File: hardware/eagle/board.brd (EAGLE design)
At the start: 91.1 x 52.6 mm, 43 parts, among them IC1 TPS61165, IC2 TPS61165, Q1 12M, U1 24AA02, X1 MINI-USB-32005-301

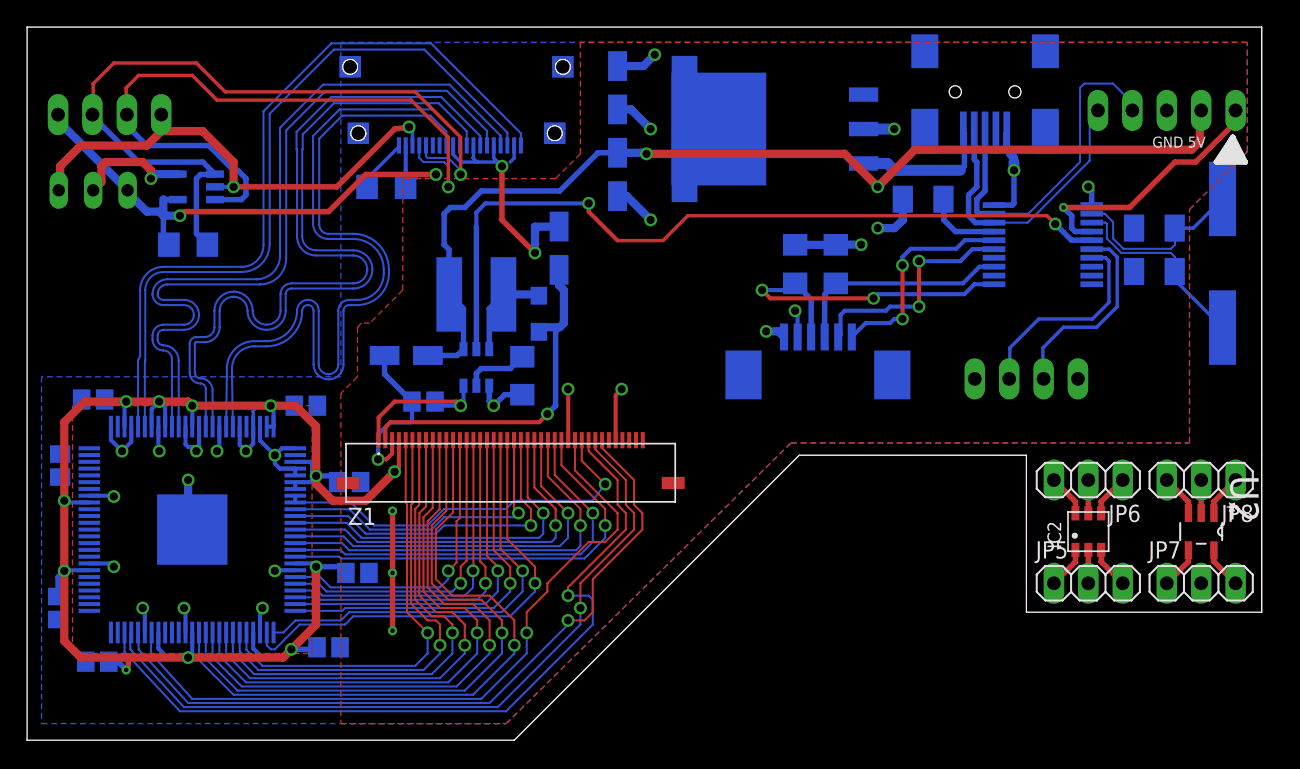
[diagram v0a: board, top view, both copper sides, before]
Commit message: Update Eagle files
Tweaked design to shrink the PCB, remove
backlight buttons, and removed the diode
on MCLR for the microcontroller.
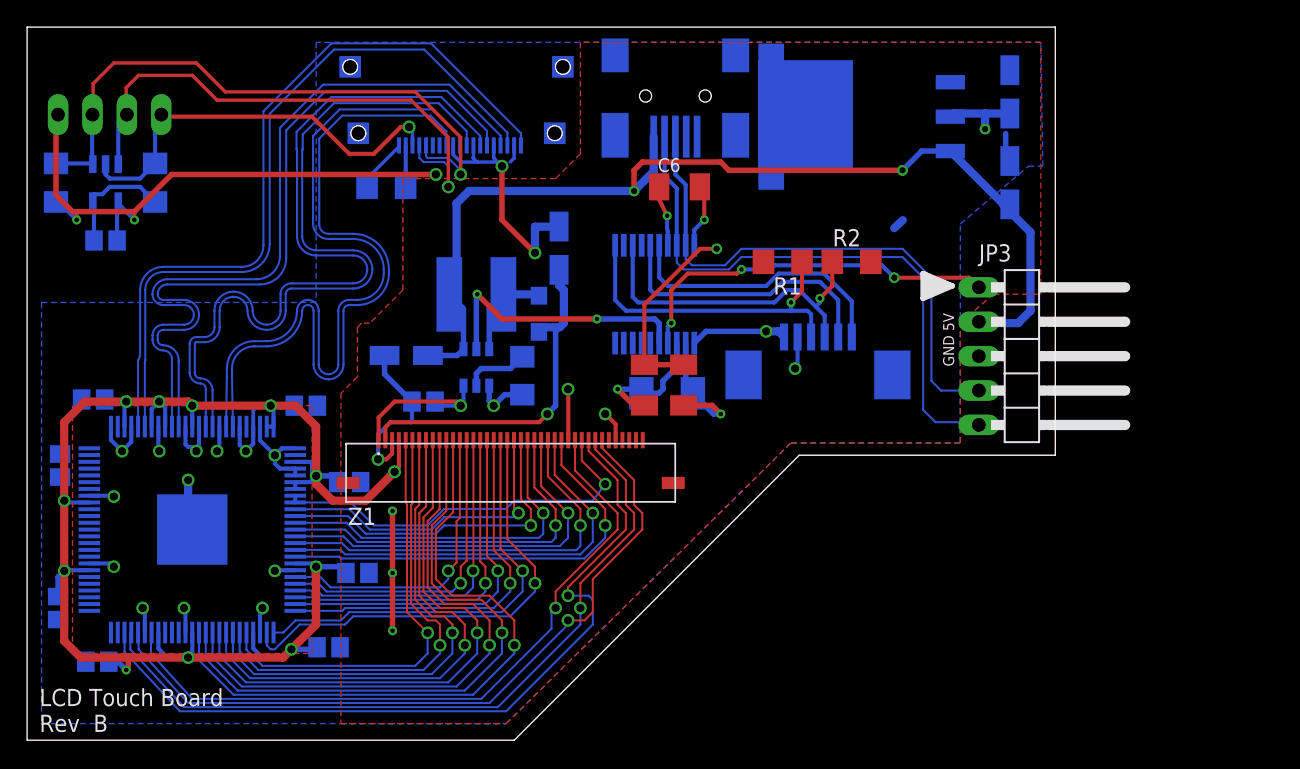
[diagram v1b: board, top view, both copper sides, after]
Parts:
- removed IC2: TPS61165, ic:SOT-23-6
- removed JP2: (no value), jumper:JP2W
- removed JP4: (no value), pinhead:1X04/90
- removed JP5, JP6, JP7, JP8: (no value), pinhead:1X03
- removed Q1: 12M, crystal:CSM-7X-DU
- removed U2: (no value), Microchip-24AA02E64T-I_OT:SOT95P270X145-5N
- added R3: 0, resistor:R0805
- added R7: 47k, resistor:R1206
- added X2: 12k, ic:CTS-445
- moved C4 38.6 mm to (45.9, 49.1), flipped to the top, turned to 90 degrees
- moved C5 36.6 mm to (48.8, 49.1), flipped to the top, turned to 90 degrees
- moved C8 29.0 mm to (72.8, 64.0), turned to 270 degrees
- moved C7 29.0 mm to (72.8, 70.7), turned to 270 degrees
- moved U$1 28.9 mm to (46.6, 55.8), turned to 90 degrees
- moved JP3 24.1 mm to (74.4, 51.2), flipped to the top, turned to 270 degrees
- moved X1 22.9 mm to (48.2, 70.4)
- moved C6 18.0 mm to (48.5, 63.7), flipped to the top
- moved R5 10.8 mm to (2.44, 64.0), turned to 90 degrees
- moved U1 6.71 mm to (6.10, 64.0), turned to 270 degrees
- moved U$2 6.47 mm to (61.3, 68.9)
- moved R2 1.17 mm to (61.2, 58.2), flipped to the top, turned to 0 degrees
- moved R1 0.93 mm to (56.1, 58.2), flipped to the top, turned to 180 degrees
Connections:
- removed net BL_DN: JP4.3, U$1.6
- removed net BL_UP: JP4.2, U$1.7
- removed net N$10: JP8.2, U2.2
- removed net N$11: JP8.3, U2.3
- removed net N$12: JP7.1, U2.4
- removed net N$13: JP7.3, U2.5
- removed net N$3: IC2.1, JP5.1
- removed net N$4: IC2.2, JP5.2
- removed net N$5: IC2.3, JP5.3
- removed net N$6: IC2.6, JP6.3
- removed net N$7: IC2.5, JP6.2
- removed net N$8: IC2.4, JP6.1
- removed net N$9: JP8.1, U2.1
- net 3V3: no longer JP4.1
- net EDID_GND: now also R7.1; no longer JP2.1
- net EDID_VCC: now also R3.1; no longer JP2.3
- net EDID_WP: now also R3.2, R7.2; no longer JP2.2
- net GND: no longer JP4.4
- net N$1: now also X2.X1; no longer Q1.1
- net N$2: now also X2.X2; no longer Q1.2
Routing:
- net BL_BRIGHT: track 58.8 -> 20.2 mm
- net PGC: track 22.0 -> 43.4 mm
- net BL_UP: track 15.4 -> 0.00 mm
- net BL_DN: track 14.8 -> 0.00 mm
- net PGD: track 26.0 -> 40.5 mm
- net EDID_SCL: track 56.8 -> 45.5 mm
- net EDID_SDA: track 51.6 -> 40.5 mm
- net 5V: track 88.1 -> 77.6 mm
- net MCLR: track 19.5 -> 28.2 mm, vias 1 -> 3
- net T_SDA: track 16.5 -> 24.7 mm, vias 0 -> 1
- net EDID_GND: track 37.3 -> 30.6 mm, vias 2 -> 1
- net EDID_VCC: track 42.9 -> 49.5 mm, vias 2 -> 3
- net N$1: track 14.5 -> 9.91 mm, vias 0 -> 1
- net T_WAKE: track 16.1 -> 20.7 mm, vias 2 -> 0
- net N$2: track 13.7 -> 9.63 mm, vias 0 -> 1
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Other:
- board size 91.1 x 52.6 mm -> 75.9 x 52.6 mm
- board text added: "LCD Touch Board Rev B"
- board text added: "WP"

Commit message: Shrank circuit again.
Circuit board is smaller now, and also has the proper
wiring for low voltage programming. The missing resistor
was causing unexpected reboots of the device.
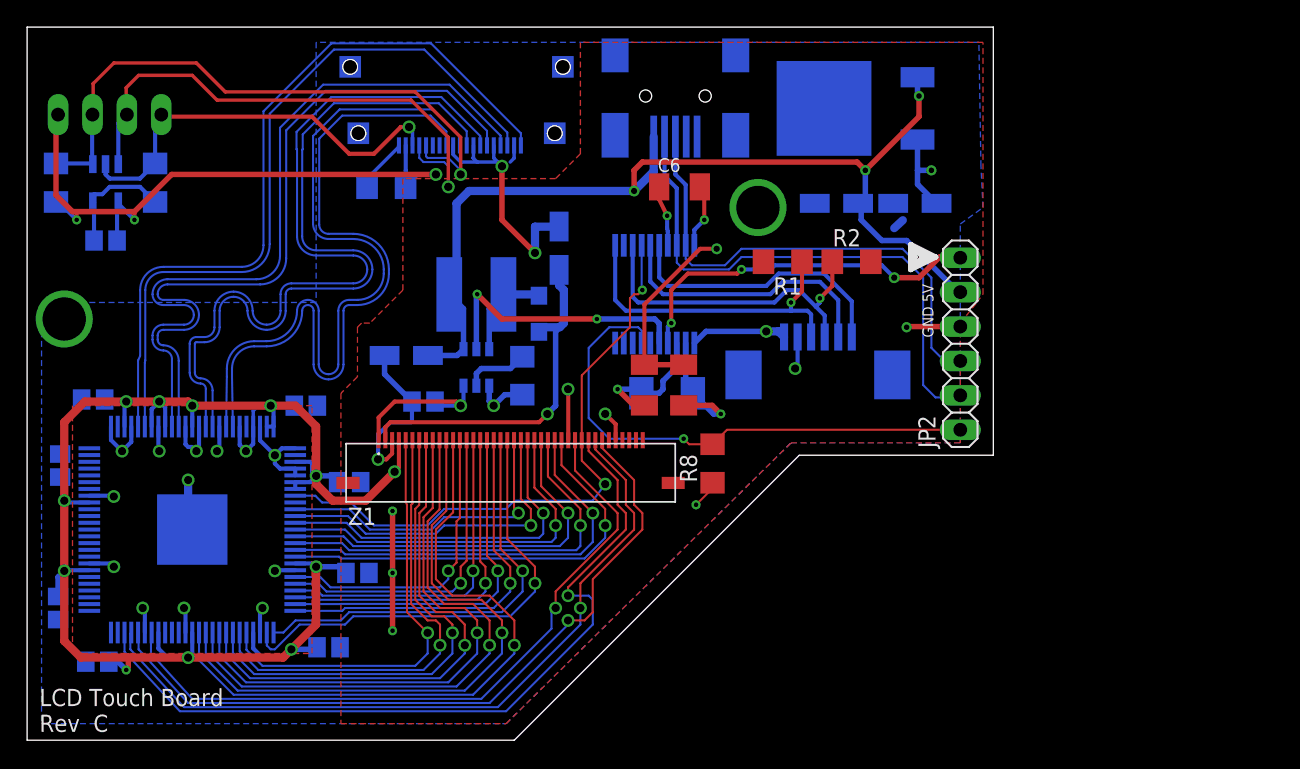
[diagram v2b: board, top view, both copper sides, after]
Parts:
- removed JP3: (no value), pinhead:1X05/90
- removed U$2: LM1086, lm1086:TO-263
- added JP2: (no value), pinhead:1X06
- added R8: 10k, resistor:R1206
- added U$5: AP7363TO252, ap7363:TO252
- moved C8 12.9 mm to (60.0, 62.5), turned to 180 degrees
- moved C7 10.8 mm to (65.8, 62.5), turned to 180 degrees
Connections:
- new net PGM: JP2.1, R8.2, U$1.7
- net 3V3: now also U$5.3; no longer U$2.2
- net 5V: now also JP2.5, U$5.1; no longer JP3.2, U$2.3
- net GND: now also JP2.4, R8.1, U$5.2_TAB; no longer JP3.3, U$2.1
- net LCD_STBY: now also U$1.14; no longer U$3.P$9
- net MCLR: now also JP2.6; no longer JP3.1
- net PGC: now also JP2.2; no longer JP3.5
- net PGD: now also JP2.3; no longer JP3.4
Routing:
- net PGM: track 0.00 -> 39.5 mm, vias 0 -> 1
- net LCD_STBY: track 29.4 -> 45.6 mm, vias 1 -> 2
- net GND: track 110.5 -> 114.3 mm, vias 24 -> 26
- net PGD: track 40.5 -> 36.8 mm
- net 5V: track 77.6 -> 74.0 mm, vias 2 -> 3
- net PGC: track 43.4 -> 40.2 mm
- net MCLR: track 28.2 -> 27.1 mm
- net 3V3: track 139.8 -> 140.5 mm
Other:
- board size 75.9 x 52.6 mm -> 71.3 x 52.6 mm
- board text added: "LCD Touch Board Rev C"
- board text removed: "LCD Touch Board Rev B"
